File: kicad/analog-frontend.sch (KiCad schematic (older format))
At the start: 28 parts, among them J1 IRON_TIP, Q1 SIA483DJ-T1-GE3, Q2 FDG6301N_F085, Q6 MMBT3906WT1G, Q7 FDG6301N_F085, U1 ACS711xEX, U2 MCP6V71U, U8 TLV1701

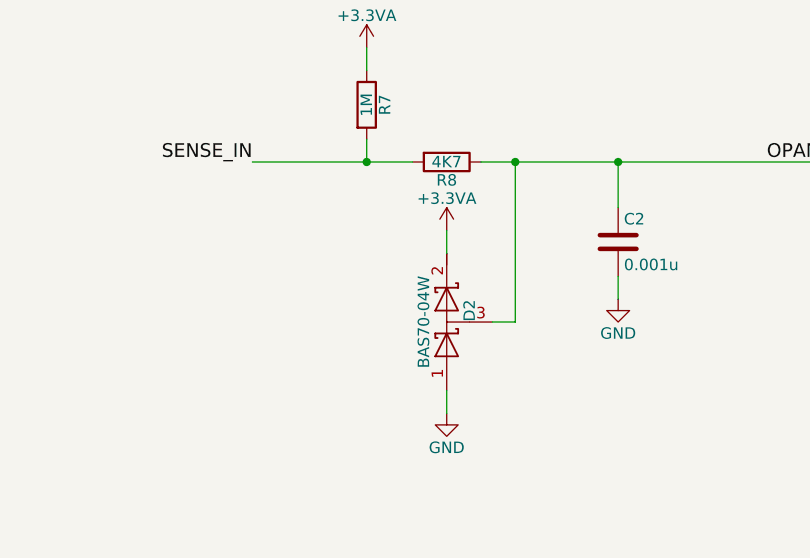
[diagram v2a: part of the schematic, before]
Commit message: Fixed some capacitor footprints
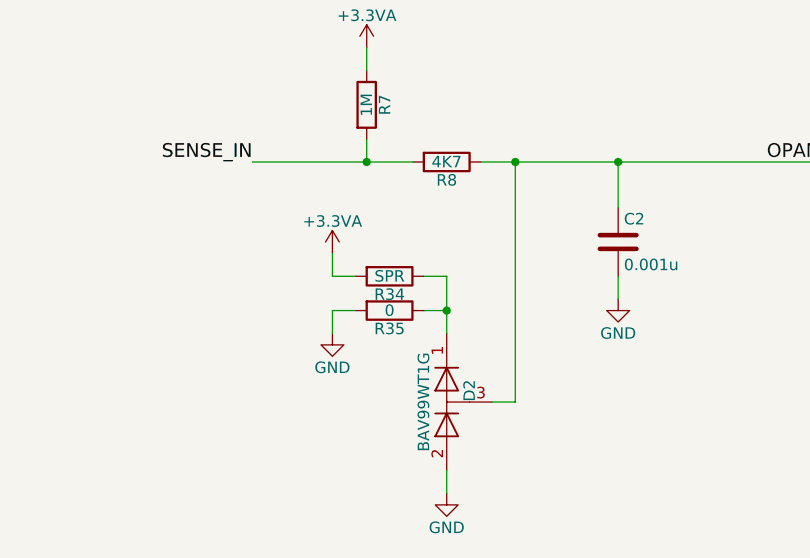
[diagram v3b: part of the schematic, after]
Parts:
- removed D2: BAS70-04W, TO_SOT_Packages_SMD:SOT-323_SC-70, symbol D_Schottky_x2_Serial_AKC
- added D2: BAV99WT1G, TO_SOT_Packages_SMD:SOT-323_SC-70, symbol D_x2_Serial_KAC
- added R34: SPR, Resistors_SMD:R_0402, symbol R
- added R35: 0, Resistors_SMD:R_0402, symbol R
- C1, C2: footprint Resistors_SMD:R_0402 -> Capacitors_SMD:C_0402
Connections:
- net +3.3VA: now also R34.2
- net GND: now also D2.2 (A), R35.2
- net OPAMP_SENSE_IN: now also D2.3 (common)
- new net: D2.1 (K), R34.1, R35.1
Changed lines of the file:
@@
 F 0 "C2" H 4925 6350 50  0000 L CNN
 F 1 "0.001u" H 4925 6150 50  0000 L CNN
-F 2 "Resistors_SMD:R_0402" H 4938 6100 50  0001 C CNN
+F 2 "Capacitors_SMD:C_0402" H 4938 6100 50  0001 C CNN
 F 3 "" H 4900 6250 50  0001 C CNN
 F 4 "1276-1057-1-ND" H 4900 6250 60  0001 C CNN "Part No."
@@
 F 0 "C1" H 8725 6150 50  0000 L CNN
 F 1 "0.001u" H 8725 5950 50  0000 L CNN
-F 2 "Resistors_SMD:R_0402" H 8738 5900 50  0001 C CNN
+F 2 "Capacitors_SMD:C_0402" H 8738 5900 50  0001 C CNN
 F 3 "" H 8700 6050 50  0001 C CNN
 F 4 "1276-1057-1-ND" H 8700 6050 60  0001 C CNN "Part No."
@@
 $EndComp
 $Comp
-L D_Schottky_x2_Serial_AKC D2
-U 1 1 5930F74A
-P 4150 6600
-F 0 "D2" H 4200 6500 50  0000 C CNN
-F 1 "BAS70-04W" H 4150 6700 50  0000 C CNN
-F 2 "TO_SOT_Packages_SMD:SOT-323_SC-70" H 4150 6600 50  0001 C CNN
-F 3 "" H 4150 6600 50  0001 C CNN
-F 4 "1727-3563-1-ND" H 4150 6600 60  0001 C CNN "Part No."
-	1    4150 6600
-	0    -1   -1   0
-$EndComp
-$Comp
 L +3.3VA #PWR017
 U 1 1 5930F993
-P 4150 6200
-F 0 "#PWR017" H 4150 6050 50  0001 C CNN
-F 1 "+3.3VA" H 4150 6340 50  0000 C CNN
-F 2 "" H 4150 6200 50  0001 C CNN
-F 3 "" H 4150 6200 50  0001 C CNN
-	1    4150 6200
+P 3650 6300
+F 0 "#PWR017" H 3650 6150 50  0001 C CNN
+F 1 "+3.3VA" H 3650 6440 50  0000 C CNN
+F 2 "" H 3650 6300 50  0001 C CNN
+F 3 "" H 3650 6300 50  0001 C CNN
+	1    3650 6300
 	1    0    0    -1
 $EndComp
@@
 L GND #PWR018
 U 1 1 5930FA31
-P 4150 7000
-F 0 "#PWR018" H 4150 6750 50  0001 C CNN
-F 1 "GND" H 4150 6850 50  0000 C CNN
-F 2 "" H 4150 7000 50  0001 C CNN
-F 3 "" H 4150 7000 50  0001 C CNN
-	1    4150 7000
+P 4150 7350
+F 0 "#PWR018" H 4150 7100 50  0001 C CNN
+F 1 "GND" H 4150 7200 50  0000 C CNN
+F 2 "" H 4150 7350 50  0001 C CNN
+F 3 "" H 4150 7350 50  0001 C CNN
+	1    4150 7350
 	1    0    0    -1
 $EndComp
@@
 Connection ~ 9200 1400
 Wire Wire Line
-	4150 6200 4150 6300
-Wire Wire Line
-	4150 7000 4150 6900
-Wire Wire Line
-	4350 6600 4450 6600
-Wire Wire Line
-	4450 6600 4450 5900
+	3650 6300 3650 6400
+Wire Wire Line
+	4150 7350 4150 7250
+Wire Wire Line
+	4350 6950 4450 6950
+Wire Wire Line
+	4450 6950 4450 5900
 Connection ~ 4450 5900
 Wire Wire Line
@@
 Text Notes 1700 2850 0    60   ~ 0
 U8 was chosen for its high output voltage tolerance
+$Comp
+L D_x2_Serial_KAC D2
+U 1 1 59D1D460
+P 4150 6950
+F 0 "D2" H 4200 6850 50  0000 C CNN
+F 1 "BAV99WT1G" H 4150 7050 50  0000 C CNN
+F 2 "TO_SOT_Packages_SMD:SOT-323_SC-70" H 4150 6950 50  0001 C CNN
+F 3 "" H 4150 6950 50  0001 C CNN
+F 4 "BAV99WT1GOSCT-ND" H 4150 6950 60  0001 C CNN "Part No."
+	1    4150 6950
+	0    -1   -1   0
+$EndComp
+$Comp
+L R R34
+U 1 1 59D1D623
+P 3900 6400
+F 0 "R34" V 3980 6400 50  0000 C CNN
+F 1 "SPR" V 3900 6400 50  0000 C CNN
+F 2 "Resistors_SMD:R_0402" V 3830 6400 50  0001 C CNN
+F 3 "" H 3900 6400 50  0001 C CNN
+	1    3900 6400
+	0    1    1    0
+$EndComp
+$Comp
+L R R35
+U 1 1 59D1D6E8
+P 3900 6550
+F 0 "R35" V 3980 6550 50  0000 C CNN
+F 1 "0" V 3900 6550 50  0000 C CNN
+F 2 "Resistors_SMD:R_0402" V 3830 6550 50  0001 C CNN
+F 3 "" H 3900 6550 50  0001 C CNN
+F 4 "311-0.0JRCT-ND" H 3900 6550 60  0001 C CNN "Part No."
+	1    3900 6550
+	0    1    1    0
+$EndComp
+Wire Wire Line
+	4050 6400 4150 6400
+Wire Wire Line
+	4150 6400 4150 6650
+Wire Wire Line
+	3650 6400 3750 6400
+Wire Wire Line
+	4050 6550 4150 6550
+Connection ~ 4150 6550
+$Comp
+L GND #PWR023
+U 1 1 59D1E7A5
+P 3650 6650
+F 0 "#PWR023" H 3650 6400 50  0001 C CNN
+F 1 "GND" H 3650 6500 50  0000 C CNN
+F 2 "" H 3650 6650 50  0001 C CNN
+F 3 "" H 3650 6650 50  0001 C CNN
+	1    3650 6650
+	1    0    0    -1
+$EndComp
+Wire Wire Line
+	3650 6650 3650 6550
+Wire Wire Line
+	3650 6550 3750 6550
 $EndSCHEMATC

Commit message: Updated parts for rev B parts order, updated dates
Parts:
- Q2, Q7: Part No. FDG6301N_F085CT-ND -> FDG6301N-F085CT-ND
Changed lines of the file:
@@
 Sheet 2 4
 Title "RT Soldering Iron"
-Date "2017-06-02"
-Rev "A"
+Date "2017-11-06"
+Rev "B"
 Comp "Kevin Cuzner"
 Comment1 ""
@@
 F 2 "TO_SOT_Packages_SMD:SOT-363_SC-70-6" H 3500 2300 50  0001 C CNN
 F 3 "" H 3300 2200 50  0001 C CNN
-F 4 "FDG6301N_F085CT-ND" H 3300 2200 60  0001 C CNN "Part No."
+F 4 "FDG6301N-F085CT-ND" H 3300 2200 60  0001 C CNN "Part No."
 	2    3300 2200
 	-1   0    0    -1
@@
 F 2 "TO_SOT_Packages_SMD:SOT-363_SC-70-6" H 5000 2200 50  0001 C CNN
 F 3 "" H 4800 2100 50  0001 C CNN
-F 4 "FDG6301N_F085CT-ND" H 4800 2100 60  0001 C CNN "Part No."
+F 4 "FDG6301N-F085CT-ND" H 4800 2100 60  0001 C CNN "Part No."
 	1    4800 2100
 	1    0    0    -1
@@
 F 2 "TO_SOT_Packages_SMD:SOT-363_SC-70-6" H 2900 4200 50  0001 C CNN
 F 3 "" H 2700 4100 50  0001 C CNN
-F 4 "FDG6301N_F085CT-ND" H 2700 4100 60  0001 C CNN "Part No."
+F 4 "FDG6301N-F085CT-ND" H 2700 4100 60  0001 C CNN "Part No."
 	1    2700 4100
 	1    0    0    -1
@@
 F 2 "TO_SOT_Packages_SMD:SOT-363_SC-70-6" H 6800 3500 50  0001 C CNN
 F 3 "" H 6600 3400 50  0001 C CNN
-F 4 "FDG6301N_F085CT-ND" H 6600 3400 60  0001 C CNN "Part No."
+F 4 "FDG6301N-F085CT-ND" H 6600 3400 60  0001 C CNN "Part No."
 	2    6600 3400
 	1    0    0    -1

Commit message: Fixed a really dumb part number mistake on the comparator
The comparator part number is ths SOT23 footprint. I had planned for the
SC-70 footprint. I bought the wrong footprint...
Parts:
- U8: Part No. 296-40599-1-ND -> 296-40600-1-ND
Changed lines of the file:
@@
 F 2 "TO_SOT_Packages_SMD:SOT-353_SC-70-5" H 2000 2200 60  0001 C CNN
 F 3 "" H 2000 2200 60  0001 C CNN
-F 4 "296-40599-1-ND" H 2000 2200 60  0001 C CNN "Part No."
+F 4 "296-40600-1-ND" H 2000 2200 60  0001 C CNN "Part No."
 	1    2000 2200
 	1    0    0    -1

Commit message: Added note with conversion and amplification factors to schematic
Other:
- note added: "Gain of 371.3 gives\n15.026mV/C"
- note added: "K-type thermocouple:\nSeebeck coefficient is 40.46uV/C"
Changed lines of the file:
@@
 Wire Wire Line
 	3650 6550 3750 6550
+Text Notes 1850 6150 0    60   ~ 0
+K-type thermocouple:\nSeebeck coefficient is 40.46uV/C
+Text Notes 9300 6100 0    60   ~ 0
+Gain of 371.3 gives\n15.026mV/C
 $EndSCHEMATC
